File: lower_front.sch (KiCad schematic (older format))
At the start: 2 parts, among them U1 COMPRESSOR

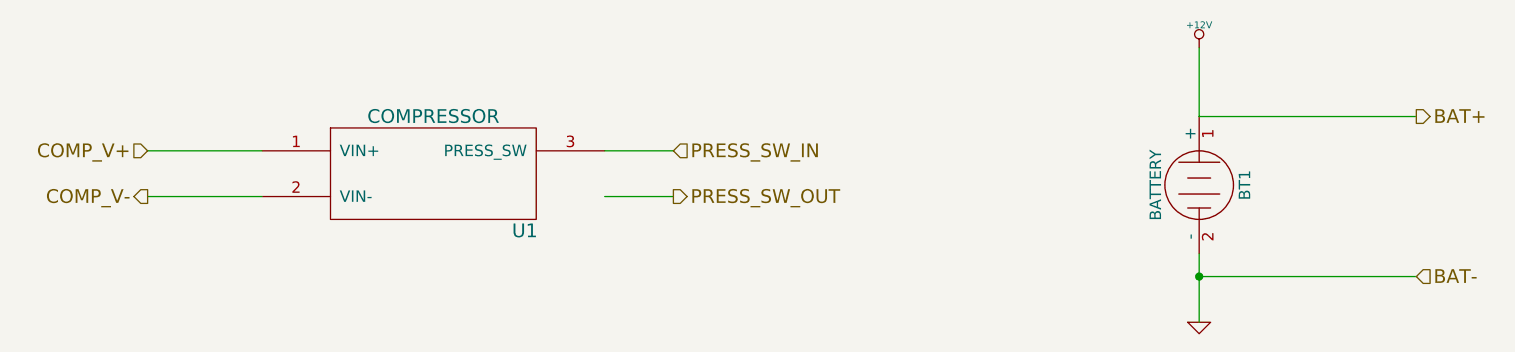
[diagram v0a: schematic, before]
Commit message: Udpates to main board and start of connector spec.
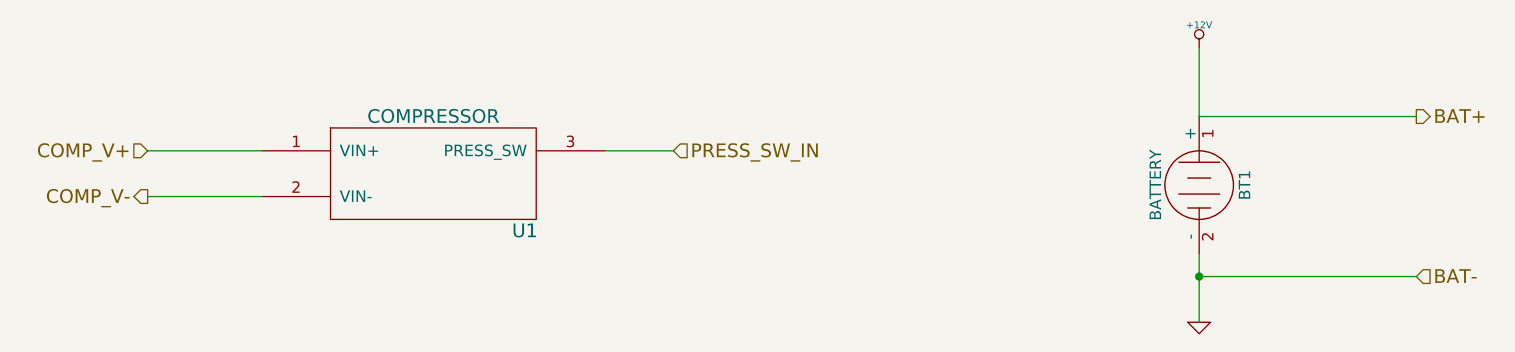
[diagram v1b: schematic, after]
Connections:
- net labels removed: PRESS_SW_OUT
- wire segments 8 -> 7
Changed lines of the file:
@@
 $Descr A4 11693 8268
 encoding utf-8
-Sheet 5 5
+Sheet 2 5
 Title ""
 Date "6 feb 2014"
@@
 Text HLabel 6050 2550 2    60   Input ~ 0
 PRESS_SW_IN
-Text HLabel 6050 2750 2    60   Output ~ 0
-PRESS_SW_OUT
 Text HLabel 3750 2550 0    60   Input ~ 0
 COMP_V+
@@
 Wire Wire Line
 	5750 2550 6050 2550
-Wire Wire Line
-	5750 2750 6050 2750
 $EndSCHEMATC
